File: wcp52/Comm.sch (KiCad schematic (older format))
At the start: 21 parts, among them J6 MicroUSB-B, Q1 IRLML6402, U1 FT230XS_DNP

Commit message: Prepare to fab
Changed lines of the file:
@@
 	1450 4000 2650 4000
 Wire Wire Line
-	2850 4000 3000 4000
+	2850 4000 6400 4000
 Wire Wire Line
-	3000 4000 5500 4000
-Wire Wire Line
-	5500 4000 6400 4000
-Wire Wire Line
-	2850 4100 3300 4100
-Wire Wire Line
-	3300 4100 5400 4100
-Wire Wire Line
-	5400 4100 6400 4100
+	2850 4100 6400 4100
 Wire Wire Line
 	3150 4900 3150 4850
@@
 	1800 4300 1450 4300
 Wire Wire Line
-	1500 4400 1500 4900
-Wire Wire Line
-	1500 4900 1500 4950
+	1500 4400 1500 4950
 Wire Wire Line
 	1300 4950 1300 4900
@@
 	2000 4950 2000 3900
 Wire Wire Line
-	1450 3900 2000 3900
-Wire Wire Line
-	2000 3900 2300 3900
+	1450 3900 2300 3900
 Wire Wire Line
 	2000 5200 2000 5150
@@
 Connection ~ 2000 3900
 Wire Wire Line
-	2900 3200 3050 3200
+	2900 3200 3750 3200
 Wire Wire Line
-	3050 3200 3150 3200
-Wire Wire Line
-	3150 3200 3550 3200
-Wire Wire Line
-	3550 3200 3750 3200
-Wire Wire Line
-	3950 3200 4400 3200
-Wire Wire Line
-	4400 3200 4700 3200
-Wire Wire Line
-	4700 3200 5450 3200
-Wire Wire Line
-	5450 3200 7700 3200
-Wire Wire Line
-	7700 3200 7900 3200
-Wire Wire Line
-	7900 3200 9500 3200
+	3950 3200 9500 3200
 Wire Wire Line
 	7700 3200 7700 3600
@@
 Connection ~ 5450 3200
 Wire Wire Line
-	6100 3800 6200 3800
-Wire Wire Line
-	6200 3800 6300 3800
-Wire Wire Line
-	6300 3800 6400 3800
+	6100 3800 6400 3800
 Wire Wire Line
 	6300 3800 6300 3600
@@
 	7700 4800 7600 4800
 Wire Wire Line
-	9500 3900 8700 3900
-Wire Wire Line
-	8700 3900 7600 3900
+	7600 3900 9500 3900
 Wire Wire Line
 	9500 4100 7600 4100
@@
 Connection ~ 7700 3200
 Wire Wire Line
-	9500 3800 8400 3800
-Wire Wire Line
-	8400 3800 7600 3800
+	7600 3800 9500 3800
 Wire Wire Line
 	7600 4000 9500 4000
@@
 Connection ~ 3000 4000
 Wire Wire Line
-	3150 3200 3150 3550
-Wire Wire Line
-	3150 3550 3150 4400
+	3150 3200 3150 4400
 Connection ~ 3150 3200
 Wire Wire Line
@@
 Connection ~ 3150 3550
 Wire Wire Line
-	3450 3550 3550 3550
-Wire Wire Line
-	3550 3550 3850 3550
-Wire Wire Line
-	3850 3550 3950 3550
-Wire Wire Line
-	3950 3550 4200 3550
-Wire Wire Line
-	4200 3550 4400 3550
+	3450 3550 4400 3550
 Wire Wire Line
 	3850 3550 3850 3300
@@
 	4200 2700 4200 2500
 Wire Wire Line
-	4200 2500 4300 2500
-Wire Wire Line
-	4300 2500 4400 2500
+	4200 2500 4400 2500
 Wire Wire Line
 	4400 2500 4400 2700

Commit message: BOM line fixes
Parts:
- C1, C2, C3, C4, C5, C6, C7, R13, R14, R15, R16, R17: Manuf Value -> (none)
- E1: Description (none) -> FERRITE CHIP 2.2k @ 100MHz [0805]
- J6: Description (none) -> CONN USB MICRO-B FEMALE
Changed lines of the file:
@@
 EESchema Schematic File Version 2
+LIBS:Altera
+LIBS:AnalogDevices
+LIBS:Atmel
+LIBS:conn-2mm
+LIBS:conn-100mil
+LIBS:conn-cui
+LIBS:conn-fci
+LIBS:conn-linx
+LIBS:conn-molex
+LIBS:conn-tagconnect
+LIBS:conn-test
+LIBS:DiodesInc
+LIBS:display
+LIBS:_electromech
+LIBS:Fairchild
+LIBS:FTDI
+LIBS:Intersil
+LIBS:Lattice
+LIBS:_linear
+LIBS:LinearTech
+LIBS:Littelfuse
+LIBS:logic-4000
+LIBS:logic-7400
+LIBS:MACOM
+LIBS:maxim
+LIBS:mechanical
+LIBS:Microchip
+LIBS:Micron
+LIBS:NXP
+LIBS:onsemi
+LIBS:passive
+LIBS:pasv-BiTech
+LIBS:pasv-Bourns
+LIBS:pasv-cap
+LIBS:pasv-ind
+LIBS:pasv-res
+LIBS:pcb
+LIBS:power
+LIBS:_semi
+LIBS:semi-diode-1N
+LIBS:semi-diode-BA
+LIBS:semi-diode-MCC
+LIBS:semi-diode-MMB
+LIBS:semi-diode-NXP
+LIBS:semi-diode-OnSemi
+LIBS:semi-diode-Vishay
+LIBS:semi-opto-misc
+LIBS:semi-thyristor-2N
+LIBS:semi-trans-2N
+LIBS:semi-trans-AO
+LIBS:semi-trans-BC
+LIBS:semi-trans-DiodesInc
+LIBS:semi-trans-Fairchild
+LIBS:semi-trans-Infineon
+LIBS:semi-trans-IntRect
+LIBS:semi-trans-IXYS
+LIBS:semi-trans-misc
+LIBS:semi-trans-MMB
+LIBS:semi-trans-MPS
+LIBS:semi-trans-NXP
+LIBS:semi-trans-PZT
+LIBS:semi-trans-TI
+LIBS:semi-trans-TIP
+LIBS:semi-trans-Toshiba
+LIBS:silabs
+LIBS:skyworks
+LIBS:ST
+LIBS:st_ic
+LIBS:st_semi
+LIBS:supertex
+LIBS:symbol
+LIBS:TexasInstruments
+LIBS:vishay_semi
+LIBS:Xilinx
+LIBS:pasv-xtal
+LIBS:conn-te
 LIBS:wcp52-cache
 EELAYER 25 0
@@
 F 5 "Laird" H 2800 3200 60  0001 C CNN "Manuf"
 F 6 "DIST DIGIKEY 240-2562-1-ND" H 2800 3200 60  0001 C CNN "BOM"
-F 7 "E1" H 2800 3200 50  0001 C CNN "OldReference"
+F 7 "FERRITE CHIP 2.2k @ 100MHz [0805]" H 2800 3200 60  0001 C CNN "Description"
+F 8 "E1" H 2800 3200 50  0001 C CNN "OldReference"
 	1    2800 3200
 	1    0    0    -1
@@
 F 3 "" H 1150 4300 50  0000 C CNN
 F 4 "10118194-0001LF" H 1350 4600 50  0001 C CNN "PN"
-F 5 "DIST DIGIKEY 609-4618-1-ND" H 1750 5000 50  0001 C CNN "BOM"
-F 6 "FCI" H 1650 4900 50  0001 C CNN "Manuf"
-F 7 "J1" H 1250 4100 50  0001 C CNN "OldReference"
+F 5 "FCI" H 1650 4900 50  0001 C CNN "Manuf"
+F 6 "DIST DIGIKEY 609-4618-1-ND" H 1750 5000 50  0001 C CNN "BOM"
+F 7 "CONN USB MICRO-B FEMALE" H 1250 4100 60  0001 C CNN "Description"
+F 8 "J1" H 1250 4100 50  0001 C CNN "OldReference"
 	1    1250 4100
 	-1   0    0    -1
@@
 F 2 "IPC7351-Nominal:CAPC2012X70" H 5450 3400 50  0001 C CNN
 F 3 "" H 5440 3375 60  0000 C CNN
-F 4 "Value" H 5450 3400 60  0001 C CNN "Manuf"
+F 4 "" H 5450 3400 60  0001 C CNN "Manuf"
 F 5 "CAP MLCC 10u ≥X5R 10V 10% [0805]" H 6250 3950 60  0001 C CNN "BOM"
 F 6 "C92" H 5450 3400 50  0001 C CNN "OldReference"
@@
 F 2 "IPC7351-Nominal:CAPC1608X55" H 6000 3800 50  0001 C CNN
 F 3 "" H 5990 3775 60  0000 C CNN
-F 4 "Value" H 6000 3800 60  0001 C CNN "Manuf"
+F 4 "" H 6000 3800 60  0001 C CNN "Manuf"
 F 5 "CAP MLCC 100n ≥X7R 16V 10% [0603]" H 6800 4350 60  0001 C CNN "BOM"
 F 6 "C32" H 6000 3800 50  0001 C CNN "OldReference"
@@
 F 2 "IPC7351-Nominal:CAPC1608X55" H 7900 3400 50  0001 C CNN
 F 3 "" H 7890 3375 60  0000 C CNN
-F 4 "Value" H 7900 3400 60  0001 C CNN "Manuf"
+F 4 "" H 7900 3400 60  0001 C CNN "Manuf"
 F 5 "CAP MLCC 100n ≥X7R 16V 10% [0603]" H 8700 3950 60  0001 C CNN "BOM"
 F 6 "C33" H 7900 3400 50  0001 C CNN "OldReference"
@@
 F 2 "IPC7351-Nominal:CAPC1608X55" H 1300 5050 50  0001 C CNN
 F 3 "" H 1290 5025 60  0000 C CNN
-F 4 "Value" H 1300 5050 60  0001 C CNN "Manuf"
+F 4 "" H 1300 5050 60  0001 C CNN "Manuf"
 F 5 "CAP MLCC 10n ≥X5R 50V 10% [0603]" H 2100 5600 60  0001 C CNN "BOM"
 F 6 "C38" H 1300 5050 50  0001 C CNN "OldReference"
@@
 F 2 "IPC7351-Nominal:CAPC1608X55" H 2000 5050 50  0001 C CNN
 F 3 "" H 1990 5025 60  0000 C CNN
-F 4 "Value" H 2000 5050 60  0001 C CNN "Manuf"
+F 4 "" H 2000 5050 60  0001 C CNN "Manuf"
 F 5 "CAP MLCC 10n ≥X5R 50V 10% [0603]" H 2800 5600 60  0001 C CNN "BOM"
 F 6 "C39" H 2000 5050 50  0001 C CNN "OldReference"
@@
 F 2 "IPC7351-Nominal:CAPC1608X55" H 3350 3550 50  0001 C CNN
 F 3 "" H 3340 3525 60  0000 C CNN
-F 4 "Value" H 3350 3550 60  0001 C CNN "Manuf"
+F 4 "" H 3350 3550 60  0001 C CNN "Manuf"
 F 5 "CAP MLCC 100n ≥X7R 16V 10% [0603]" H 4150 4100 60  0001 C CNN "BOM"
 F 6 "C63" H 3350 3550 50  0001 C CNN "OldReference"
@@
 F 2 "IPC7351-Nominal:CAPC1608X55" H 4500 3550 50  0001 C CNN
 F 3 "" H 4490 3525 60  0000 C CNN
-F 4 "Value" H 4500 3550 60  0001 C CNN "Manuf"
+F 4 "" H 4500 3550 60  0001 C CNN "Manuf"
 F 5 "CAP MLCC 10n ≥X5R 50V 10% [0603]" H 5300 4100 60  0001 C CNN "BOM"
 F 6 "C64" H 4500 3550 50  0001 C CNN "OldReference"
@@
 F 2 "IPC7351-Nominal:RESC1608X50" H 2750 4000 50  0001 C CNN
 F 3 "" H 2750 4050 60  0000 C CNN
-F 4 "Value" H 2750 4000 60  0001 C CNN "Manuf"
+F 4 "" H 2750 4000 60  0001 C CNN "Manuf"
 F 5 "RES SMD 22 5% [0603]" H 3500 4550 60  0001 C CNN "BOM"
 F 6 "R7" H 2750 4000 50  0001 C CNN "OldReference"
@@
 F 2 "IPC7351-Nominal:RESC1608X50" H 2750 4100 50  0001 C CNN
 F 3 "" H 2750 4150 60  0000 C CNN
-F 4 "Value" H 2750 4100 60  0001 C CNN "Manuf"
+F 4 "" H 2750 4100 60  0001 C CNN "Manuf"
 F 5 "RES SMD 22 5% [0603]" H 3500 4650 60  0001 C CNN "BOM"
 F 6 "R8" H 2750 4100 50  0001 C CNN "OldReference"
@@
 F 2 "IPC7351-Nominal:RESC1608X50" H 1500 5050 50  0001 C CNN
 F 3 "" H 1500 5100 60  0000 C CNN
-F 4 "Value" H 1500 5050 60  0001 C CNN "Manuf"
+F 4 "" H 1500 5050 60  0001 C CNN "Manuf"
 F 5 "RES SMD 1M 5% [0603]" H 2250 5600 60  0001 C CNN "BOM"
 F 6 "R36" H 1500 5050 50  0001 C CNN "OldReference"
@@
 F 2 "IPC7351-Nominal:RESC1608X50" H 3950 3750 50  0001 C CNN
 F 3 "" H 3950 3800 60  0000 C CNN
-F 4 "Value" H 3950 3750 60  0001 C CNN "Manuf"
+F 4 "" H 3950 3750 60  0001 C CNN "Manuf"
 F 5 "RES SMD 1M 5% [0603]" H 4700 4300 60  0001 C CNN "BOM"
 F 6 "R16" H 3950 3750 50  0001 C CNN "OldReference"
@@
 F 2 "IPC7351-Nominal:RESC1608X50" H 3550 3400 50  0001 C CNN
 F 3 "" H 3550 3450 60  0000 C CNN
-F 4 "Value" H 3550 3400 60  0001 C CNN "Manuf"
+F 4 "" H 3550 3400 60  0001 C CNN "Manuf"
 F 5 "RES SMD 1M 5% [0603]" H 4300 3950 60  0001 C CNN "BOM"
 F 6 "R37" H 3550 3400 50  0001 C CNN "OldReference"

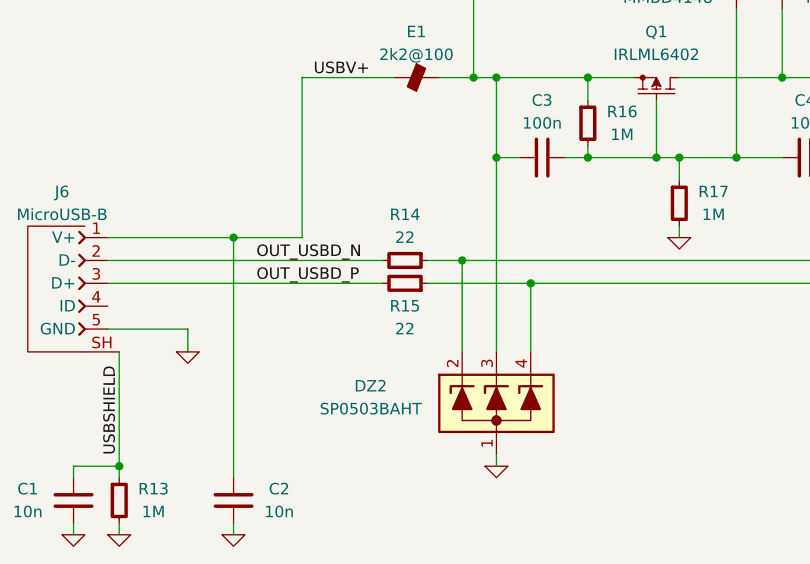
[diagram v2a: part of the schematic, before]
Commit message: BOM corrections/combinations, etc
Add configuration for bomtool
Remove old schematic file no longer used
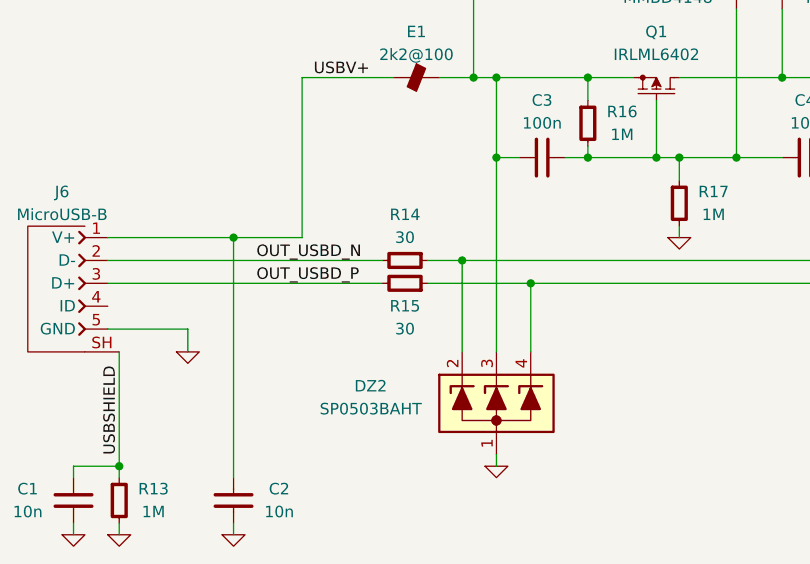
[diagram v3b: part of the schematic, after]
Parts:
- C6, C7: BOM CAP MLCC 100n ≥X7R 16V 10% [0603] -> #CAP MLCC 100n ≥X7R 16V 10% [0603]
- D3, D4: BOM (none) -> SEMI GENERIC MMBD4148
- R14, R15: value 22 -> 30; BOM RES SMD 22 5% [0603] -> RES SMD 30 1% [0603]
- U1: BOM IC FTDI FT230XS -> #IC FTDI FT230XS
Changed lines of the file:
@@
 F 4 "FT230XS-R" H 7000 4200 60  0001 C CNN "PN"
 F 5 "FTDI" H 7000 4200 60  0001 C CNN "Manuf"
-F 6 "IC FTDI FT230XS" H 7000 4200 60  0001 C CNN "BOM"
+F 6 "#IC FTDI FT230XS" H 7000 4200 60  0001 C CNN "BOM"
 F 7 "U13" H 7000 4200 50  0001 C CNN "OldReference"
 	1    7000 4200
@@
 F 2 "IPC7351-Nominal:CAPC1608X55" H 6000 3800 50  0001 C CNN
 F 3 "" H 5990 3775 60  0000 C CNN
-F 4 "" H 6000 3800 60  0001 C CNN "Manuf"
-F 5 "CAP MLCC 100n ≥X7R 16V 10% [0603]" H 6800 4350 60  0001 C CNN "BOM"
-F 6 "C32" H 6000 3800 50  0001 C CNN "OldReference"
+F 4 "#CAP MLCC 100n ≥X7R 16V 10% [0603]" H 6800 4350 60  0001 C CNN "BOM"
+F 5 "C32" H 6000 3800 50  0001 C CNN "OldReference"
 	1    6000 3800
 	0    1    1    0
@@
 F 2 "IPC7351-Nominal:CAPC1608X55" H 7900 3400 50  0001 C CNN
 F 3 "" H 7890 3375 60  0000 C CNN
-F 4 "" H 7900 3400 60  0001 C CNN "Manuf"
-F 5 "CAP MLCC 100n ≥X7R 16V 10% [0603]" H 8700 3950 60  0001 C CNN "BOM"
-F 6 "C33" H 7900 3400 50  0001 C CNN "OldReference"
+F 4 "#CAP MLCC 100n ≥X7R 16V 10% [0603]" H 8700 3950 60  0001 C CNN "BOM"
+F 5 "C33" H 7900 3400 50  0001 C CNN "OldReference"
 	1    7900 3400
 	-1   0    0    1
@@
 F 2 "smd-semi:SOT-23" H 4200 2800 50  0001 C CNN
 F 3 "" H 4200 2800 60  0000 C CNN
-F 4 "D8" H 4200 2800 50  0001 C CNN "OldReference"
+F 4 "SEMI GENERIC MMBD4148" H 4200 2800 60  0001 C CNN "BOM"
+F 5 "D8" H 4200 2800 50  0001 C CNN "OldReference"
 	1    4200 2800
 	-1   0    0    -1
@@
 F 2 "smd-semi:SOT-23" H 4400 2800 50  0001 C CNN
 F 3 "" H 4400 2800 60  0000 C CNN
-F 4 "D9" H 4400 2800 50  0001 C CNN "OldReference"
+F 4 "SEMI GENERIC MMBD4148" H 4400 2800 60  0001 C CNN "BOM"
+F 5 "D9" H 4400 2800 50  0001 C CNN "OldReference"
 	1    4400 2800
 	1    0    0    -1
@@
 P 2750 4000
 F 0 "R14" V 2550 4000 50  0000 C CNN
-F 1 "22" V 2650 4000 50  0000 C CNN
+F 1 "30" V 2650 4000 50  0000 C CNN
 F 2 "IPC7351-Nominal:RESC1608X50" H 2750 4000 50  0001 C CNN
 F 3 "" H 2750 4050 60  0000 C CNN
-F 4 "" H 2750 4000 60  0001 C CNN "Manuf"
-F 5 "RES SMD 22 5% [0603]" H 3500 4550 60  0001 C CNN "BOM"
-F 6 "R7" H 2750 4000 50  0001 C CNN "OldReference"
+F 4 "RES SMD 30 1% [0603]" H 3500 4550 60  0001 C CNN "BOM"
+F 5 "R7" H 2750 4000 50  0001 C CNN "OldReference"
 	1    2750 4000
 	0    1    1    0
@@
 P 2750 4100
 F 0 "R15" V 2650 4100 50  0000 C CNN
-F 1 "22" V 2550 4100 50  0000 C CNN
+F 1 "30" V 2550 4100 50  0000 C CNN
 F 2 "IPC7351-Nominal:RESC1608X50" H 2750 4100 50  0001 C CNN
 F 3 "" H 2750 4150 60  0000 C CNN
-F 4 "" H 2750 4100 60  0001 C CNN "Manuf"
-F 5 "RES SMD 22 5% [0603]" H 3500 4650 60  0001 C CNN "BOM"
-F 6 "R8" H 2750 4100 50  0001 C CNN "OldReference"
+F 4 "RES SMD 30 1% [0603]" H 3500 4650 60  0001 C CNN "BOM"
+F 5 "R8" H 2750 4100 50  0001 C CNN "OldReference"
 	1    2750 4100
 	0    1    -1   0

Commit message: Schematic/doc work
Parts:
- removed C1, C2: 10n, IPC7351-Nominal:CAPC1608X55, symbol C-0603
- removed J6: MicroUSB-B, conn-fci:CONN-10118194-0001LF-FCI, symbol CONN-10118194-0001LF-UUSB-B
- removed R13: 1M, IPC7351-Nominal:RESC1608X50, symbol R-0603
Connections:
- net OUT_USBD_N renamed EXT_USBD_N
- net OUT_USBD_P renamed EXT_USBD_P
- net USBD_N renamed IN_USBD_N
- net USBD_P renamed IN_USBD_P
- net USBV+ renamed EXT_VBUS
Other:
- note added: "Optional USB-UART interface\nThese parts are not normally installed."
- note added: "USB pickoff to microcontroller\nThis is the intended normal mode of communcation, rather\nthan installing the above USB-UART interface device."
- note removed: "@Q1 forms the same slew rate/inrush limiting circuit as @Q14 on\nthe "PowerInput" page.\nIf the main board power is available, @D3 allows it to force @Q1's\ngate above its source, shutting it off. @D4 then allows the main\nboard +5V rail to power the otherwise USB-powered devices,\nallowing them to draw more current."
- moved on the sheet: C5, D3, D4, E1, R14, R15

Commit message: Schematic updates for documentation
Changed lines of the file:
@@
 $EndComp
 $Comp
-L GND #PWR042
+L GND #PWR46
 U 1 1 54F70169
 P 3150 4900
-F 0 "#PWR042" H 3150 4900 30  0001 C CNN
+F 0 "#PWR46" H 3150 4900 30  0001 C CNN
 F 1 "GND" H 3150 4830 30  0001 C CNN
 F 2 "" H 3150 4900 60  0000 C CNN
@@
 $EndComp
 $Comp
-L GND #PWR047
+L GND #PWR49
 U 1 1 54F7543C
 P 5100 3600
-F 0 "#PWR047" H 5100 3600 30  0001 C CNN
+F 0 "#PWR49" H 5100 3600 30  0001 C CNN
 F 1 "GND" H 5100 3530 30  0001 C CNN
 F 2 "" H 5100 3600 60  0000 C CNN
@@
 $EndComp
 $Comp
-L GND #PWR048
+L GND #PWR50
 U 1 1 54F76B86
 P 5800 3800
-F 0 "#PWR048" H 5800 3800 30  0001 C CNN
+F 0 "#PWR50" H 5800 3800 30  0001 C CNN
 F 1 "GND" H 5800 3730 30  0001 C CNN
 F 2 "" H 5800 3800 60  0000 C CNN
@@
 $EndComp
 $Comp
-L GND #PWR049
+L GND #PWR51
 U 1 1 54F76CB4
 P 6300 4900
-F 0 "#PWR049" H 6300 4900 30  0001 C CNN
+F 0 "#PWR51" H 6300 4900 30  0001 C CNN
 F 1 "GND" H 6300 4830 30  0001 C CNN
 F 2 "" H 6300 4900 60  0000 C CNN
@@
 $EndComp
 $Comp
-L GND #PWR050
+L GND #PWR52
 U 1 1 54F76DBE
 P 7700 4900
-F 0 "#PWR050" H 7700 4900 30  0001 C CNN
+F 0 "#PWR52" H 7700 4900 30  0001 C CNN
 F 1 "GND" H 7700 4830 30  0001 C CNN
 F 2 "" H 7700 4900 60  0000 C CNN
@@
 USBPWR
 $Comp
-L GND #PWR051
+L GND #PWR53
 U 1 1 54F81F0B
 P 7900 3550
-F 0 "#PWR051" H 7900 3550 30  0001 C CNN
+F 0 "#PWR53" H 7900 3550 30  0001 C CNN
 F 1 "GND" H 7900 3480 30  0001 C CNN
 F 2 "" H 7900 3550 60  0000 C CNN
@@
 $EndComp
 $Comp
-L GND #PWR052
+L GND #PWR47
 U 1 1 54FE37FA
 P 3950 3900
-F 0 "#PWR052" H 3950 3900 30  0001 C CNN
+F 0 "#PWR47" H 3950 3900 30  0001 C CNN
 F 1 "GND" H 3950 3830 30  0001 C CNN
 F 2 "" H 3950 3900 60  0000 C CNN
@@
 $EndComp
 $Comp
-L +5 #PWR053
+L +5 #PWR48
 U 1 1 54FE450B
 P 4300 2450
-F 0 "#PWR053" H 4300 2500 30  0001 C CNN
+F 0 "#PWR48" H 4300 2500 30  0001 C CNN
 F 1 "+5" H 4300 2550 50  0000 C CNN
 F 2 "" H 4300 2450 60  0000 C CNN
@@
 VBUS
 Wire Wire Line
-	2350 4000 3000 4000
-Wire Wire Line
-	3000 4000 4400 4000
-Wire Wire Line
-	4400 4000 6400 4000
-Wire Wire Line
-	2350 4100 3300 4100
-Wire Wire Line
-	3300 4100 4300 4100
-Wire Wire Line
-	4300 4100 6400 4100
+	2350 4000 6400 4000
+Wire Wire Line
+	2350 4100 6400 4100
 Wire Wire Line
 	3150 4900 3150 4850
 Wire Wire Line
-	2350 3200 3050 3200
-Wire Wire Line
-	3050 3200 3150 3200
-Wire Wire Line
-	3150 3200 3550 3200
-Wire Wire Line
-	3550 3200 3750 3200
-Wire Wire Line
-	3950 3200 4400 3200
-Wire Wire Line
-	4400 3200 4700 3200
-Wire Wire Line
-	4700 3200 5100 3200
-Wire Wire Line
-	5100 3200 7700 3200
-Wire Wire Line
-	7700 3200 7900 3200
-Wire Wire Line
-	7900 3200 9400 3200
+	2350 3200 3750 3200
+Wire Wire Line
+	3950 3200 9400 3200
 Wire Wire Line
 	7700 3200 7700 3600
@@
 Connection ~ 5100 3200
 Wire Wire Line
-	6100 3800 6200 3800
-Wire Wire Line
-	6200 3800 6300 3800
-Wire Wire Line
-	6300 3800 6400 3800
+	6100 3800 6400 3800
 Wire Wire Line
 	6300 3800 6300 3600
@@
 	7700 4800 7600 4800
 Wire Wire Line
-	7600 3900 8700 3900
-Wire Wire Line
-	8700 3900 9400 3900
+	7600 3900 9400 3900
 Wire Wire Line
 	9400 4100 7600 4100
@@
 Connection ~ 7700 3200
 Wire Wire Line
-	7600 3800 8400 3800
-Wire Wire Line
-	8400 3800 9400 3800
+	7600 3800 9400 3800
 Wire Wire Line
 	7600 4000 9400 4000
@@
 Connection ~ 3000 4000
 Wire Wire Line
-	3150 3200 3150 3550
-Wire Wire Line
-	3150 3550 3150 4400
+	3150 3200 3150 4400
 Connection ~ 3150 3200
 Wire Wire Line
@@
 Connection ~ 3150 3550
 Wire Wire Line
-	3450 3550 3550 3550
-Wire Wire Line
-	3550 3550 3850 3550
-Wire Wire Line
-	3850 3550 3950 3550
-Wire Wire Line
-	3950 3550 4200 3550
-Wire Wire Line
-	4200 3550 4400 3550
+	3450 3550 4400 3550
 Wire Wire Line
 	3850 3550 3850 3300
@@
 	4200 2600 4200 2500
 Wire Wire Line
-	4200 2500 4300 2500
-Wire Wire Line
-	4300 2500 4400 2500
+	4200 2500 4400 2500
 Wire Wire Line
 	4400 2500 4400 2600
@@
 Text Notes 5650 6050 0    60   ~ 0
 USB pickoff to microcontroller\nThis is the intended normal mode of communcation, rather\nthan installing the above USB-UART interface device.
+$Comp
+L SIGPATH_SM #SYM44
+U 1 1 550EDEC1
+P 8100 3800
+F 0 "#SYM44" H 8100 3800 60  0001 C CNN
+F 1 "SIGPATH_SM" H 8100 3800 60  0001 C CNN
+F 2 "" H 8100 3800 60  0000 C CNN
+F 3 "" H 8100 3800 60  0000 C CNN
+	1    8100 3800
+	1    0    0    -1
+$EndComp
+$Comp
+L SIGPATH_SM #SYM45
+U 1 1 550EDEF5
+P 8100 4000
+F 0 "#SYM45" H 8100 4000 60  0001 C CNN
+F 1 "SIGPATH_SM" H 8100 4000 60  0001 C CNN
+F 2 "" H 8100 4000 60  0000 C CNN
+F 3 "" H 8100 4000 60  0000 C CNN
+	1    8100 4000
+	1    0    0    -1
+$EndComp
+$Comp
+L MSIGPATH_SM #SYM42
+U 1 1 550EDF24
+P 7950 3900
+F 0 "#SYM42" H 7950 3900 60  0001 C CNN
+F 1 "MSIGPATH_SM" H 7950 3900 60  0001 C CNN
+F 2 "" H 7950 3900 60  0000 C CNN
+F 3 "" H 7950 3900 60  0000 C CNN
+	1    7950 3900
+	-1   0    0    -1
+$EndComp
+$Comp
+L MSIGPATH_SM #SYM43
+U 1 1 550EDF58
+P 7950 4100
+F 0 "#SYM43" H 7950 4100 60  0001 C CNN
+F 1 "MSIGPATH_SM" H 7950 4100 60  0001 C CNN
+F 2 "" H 7950 4100 60  0000 C CNN
+F 3 "" H 7950 4100 60  0000 C CNN
+	1    7950 4100
+	-1   0    0    -1
+$EndComp
+$Comp
+L SIGPATH_SM #SYM46
+U 1 1 550EDF85
+P 8100 4600
+F 0 "#SYM46" H 8100 4600 60  0001 C CNN
+F 1 "SIGPATH_SM" H 8100 4600 60  0001 C CNN
+F 2 "" H 8100 4600 60  0000 C CNN
+F 3 "" H 8100 4600 60  0000 C CNN
+	1    8100 4600
+	1    0    0    -1
+$EndComp
 $EndSCHEMATC
